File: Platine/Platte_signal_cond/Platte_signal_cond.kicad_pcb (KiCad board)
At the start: 2 copper layers, 35.8 x 32.5 mm, 32 parts, among them J1 Conn_01x06, J2 Conn_01x07_MountingPin, M1 MountingHole_2.1mm, M2 MountingHole_2.1mm, M3 MountingHole_2.1mm, M4 MountingHole_2.1mm

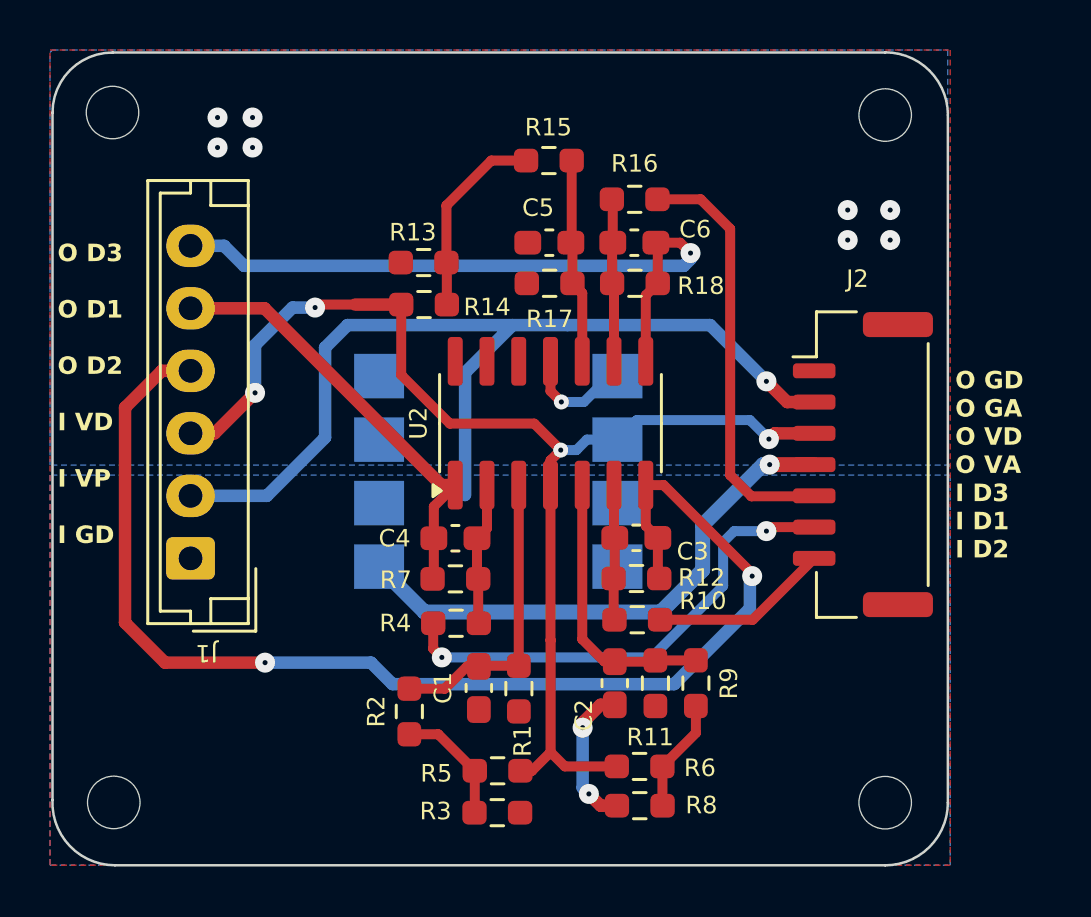
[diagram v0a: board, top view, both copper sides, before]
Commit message: Better shaping the Plates on the PCB
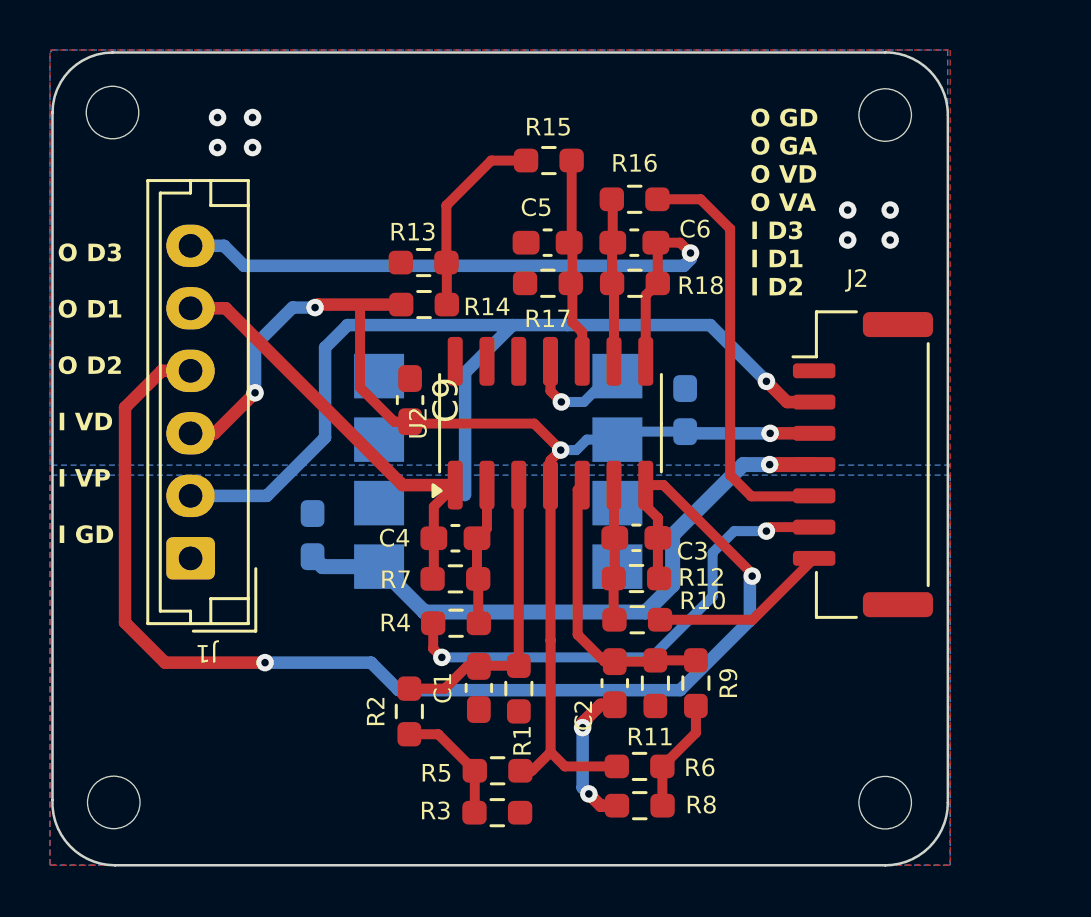
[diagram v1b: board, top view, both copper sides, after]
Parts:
- added C7: 10u, Capacitor_SMD:C_0603_1608Metric_Pad1.08x0.95mm_HandSolder, B.Cu at (116.5, 74.1)
- added C8: 10u, Capacitor_SMD:C_0603_1608Metric_Pad1.08x0.95mm_HandSolder, B.Cu at (101.6, 79.1)
- added C9: 100n, Capacitor_SMD:C_0603_1608Metric_Pad1.08x0.95mm_HandSolder, F.Cu at (105.5, 73.7)
- moved C5 0.07 mm to (111.0, 67.4)
- moved R17 0.07 mm to (111.0, 69.0)
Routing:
- net +3.3VA: track 21.6 -> 24.6 mm
- net +3.3VD: track 49.8 -> 51.2 mm
